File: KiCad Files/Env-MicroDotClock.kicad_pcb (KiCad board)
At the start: 2 copper layers, 90 x 65.2 mm, 47 parts, among them IC1 IS31FL3730-QFLS2-TR, IC2 IS31FL3730-QFLS2-TR, IC3 IS31FL3730-QFLS2-TR, IC4 IS31FL3730-QFLS2-TR, M1 Dip-14 Socket, M2 Dip-14 Socket, M3 Dip-14 Socket, M4 Dip-14 Socket, M5 Dip-14 Socket, M6 Dip-14 Socket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

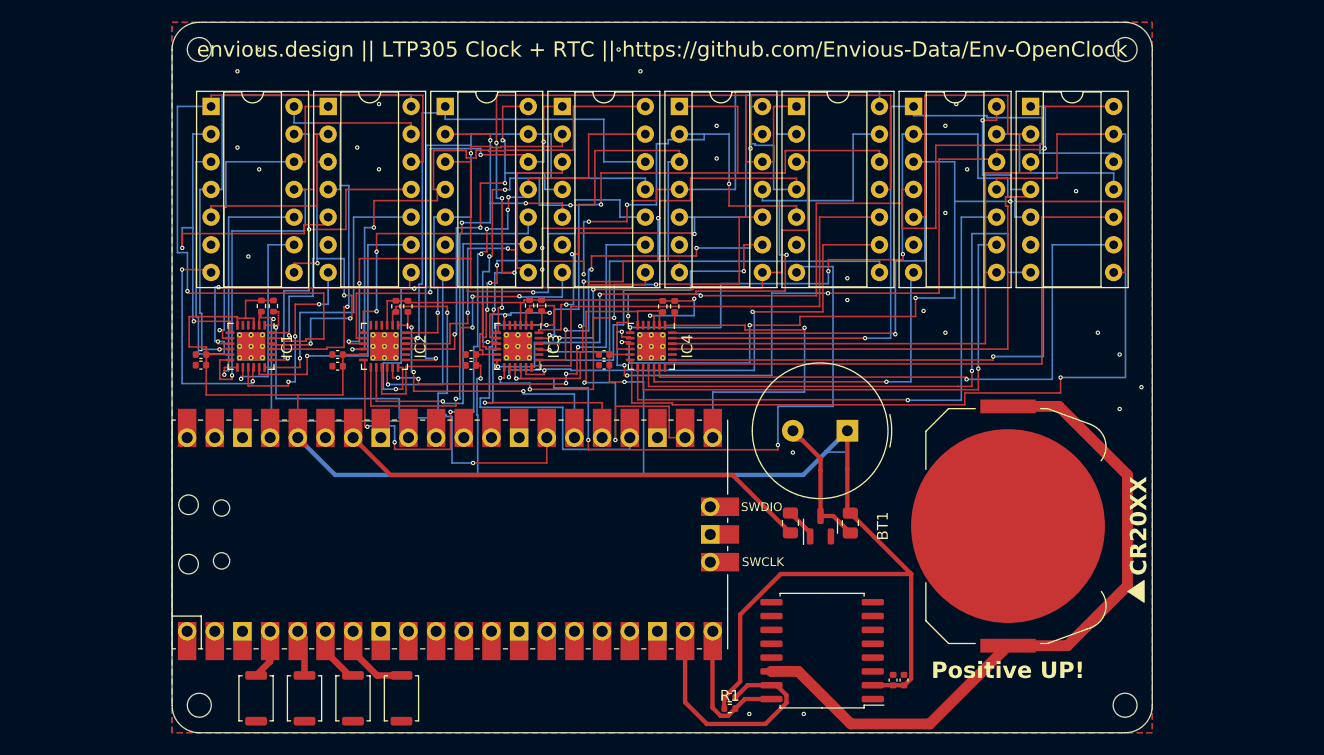
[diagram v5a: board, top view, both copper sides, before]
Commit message: aligned and organized components on main variant
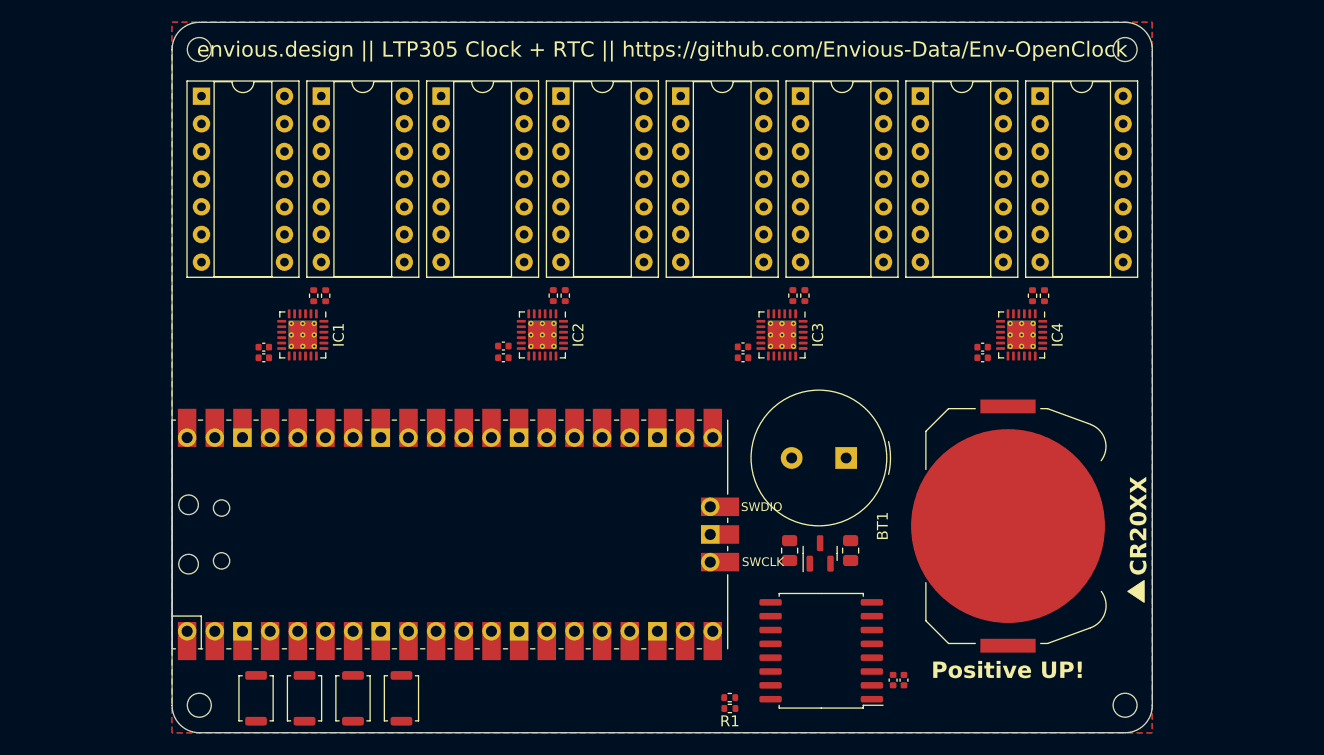
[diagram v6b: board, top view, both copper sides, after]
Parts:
- moved C7 34.8 mm to (159.4, 87.3)
- moved C8 34.8 mm to (159.4, 88.3)
- moved IC4 34.0 mm to (163.0, 86.2)
- moved R5 34.0 mm to (165.1, 82.6)
- moved R6 34.0 mm to (164.0, 82.6)
- moved C5 25.0 mm to (137.4, 87.3)
- moved C6 25.0 mm to (137.4, 88.3)
- moved IC3 24.3 mm to (141.0, 86.2)
- moved R7 24.2 mm to (143.1, 82.6)
- moved R8 24.2 mm to (142.0, 82.6)
- moved C3 15.2 mm to (115.4, 87.2)
- moved C4 15.2 mm to (115.4, 88.3)
- moved IC2 14.5 mm to (119.0, 86.2)
- moved R12 14.5 mm to (120.0, 82.6)
- moved R11 14.5 mm to (121.1, 82.6)
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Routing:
- net +3V3: track 236.2 -> 0.00 mm, vias 4 -> 0
- net IC4R5: track 91.4 -> 0.00 mm, vias 1 -> 0
- net IC4R3: track 78.8 -> 0.00 mm, vias 4 -> 0
- net IC4R4: track 76.3 -> 0.00 mm, vias 2 -> 0
- net IC3R3: track 73.6 -> 0.00 mm, vias 4 -> 0
- net IC4R2: track 71.4 -> 0.00 mm, vias 5 -> 0
- net IC1C2: track 70.8 -> 0.00 mm, vias 1 -> 0
- net IC3C5: track 67.5 -> 0.00 mm, vias 4 -> 0
- net IC4C2: track 67.2 -> 0.00 mm, vias 1 -> 0
- net IC4C5: track 67.0 -> 0.00 mm, vias 1 -> 0
- net IC3R2: track 65.6 -> 0.00 mm, vias 4 -> 0
- net Net-(BT1-+): track 63.7 -> 0.00 mm
- net IC2R5: track 63.2 -> 0.00 mm, vias 7 -> 0
- net IC4R1: track 62.7 -> 0.00 mm, vias 3 -> 0
- net IC3R4: track 62.7 -> 0.00 mm, vias 4 -> 0
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
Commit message: overhauled PCB traces and deleted old production files
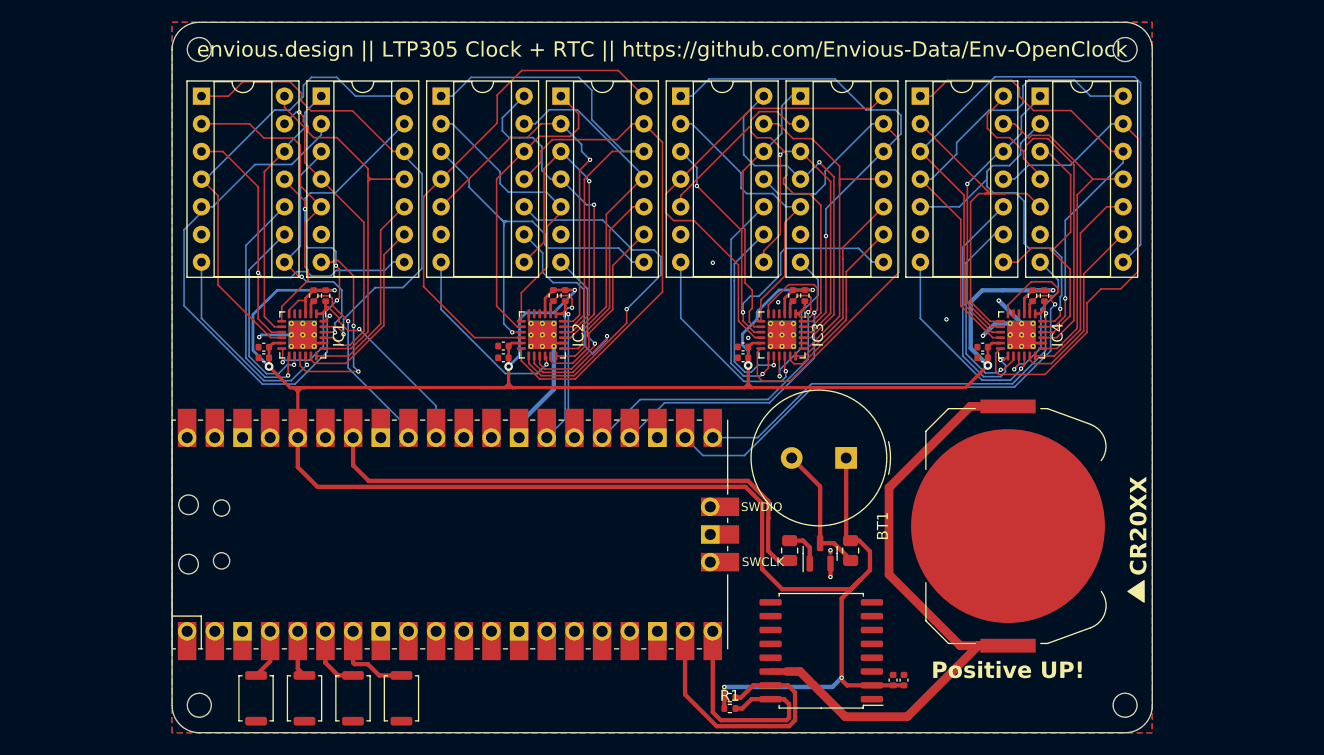
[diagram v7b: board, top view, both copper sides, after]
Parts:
- turned R1 to 0 degrees
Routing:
- net +3V3: track 0.00 -> 274.9 mm, vias 0 -> 10
- net Net-(BT1-+): track 0.00 -> 61.8 mm
- net IC4R3: track 0.00 -> 60.5 mm
- net I2C4_SCL: track 0.00 -> 54.5 mm, vias 0 -> 1
- net IC3R5: track 0.00 -> 49.2 mm
- net Buzzer GPIO: track 0.00 -> 48.9 mm
- net IC4R5: track 0.00 -> 48.2 mm
- net IC2R5: track 0.00 -> 47.9 mm
- net IC2R4: track 0.00 -> 46.7 mm
- net IC1C2: track 0.00 -> 46.4 mm, vias 0 -> 1
- net IC1C1: track 0.00 -> 46.2 mm, vias 0 -> 1
- net IC3C2: track 0.00 -> 45.9 mm, vias 0 -> 1
- net IC2C2: track 0.00 -> 45.1 mm
- net IC4R4: track 0.00 -> 42.6 mm
- net IC4C2: track 0.00 -> 42.2 mm, vias 0 -> 1
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
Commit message: fixed up some issues I saw, general improvements and adjustments to PCB
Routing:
- net IC2R2: track 27.8 -> 32.7 mm, vias 0 -> 1
- net IC3R4: track 41.9 -> 44.7 mm
- net IC4C5: track 31.5 -> 34.3 mm
- net IC2C1: track 34.9 -> 37.3 mm
- net IC4C6: track 18.9 -> 20.9 mm
- net IC2C8: track 17.6 -> 19.5 mm
- net +3V3: track 274.9 -> 276.8 mm
- net IC3R7: track 17.9 -> 19.7 mm
- net IC3R6: track 20.9 -> 22.7 mm
- net IC4R5: track 48.2 -> 49.9 mm
- net IC4C7: track 17.1 -> 18.6 mm
- net I2C4_SDA: track 39.6 -> 40.9 mm
- net IC3R3: track 37.5 -> 36.2 mm
- net I2C4_SCL: track 54.5 -> 55.6 mm
- net IC3C1: track 39.6 -> 40.7 mm
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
